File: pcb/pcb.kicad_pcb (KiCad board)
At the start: 2 copper layers, 30 parts, among them J1 Barrel_Jack_Switch, Q1 RQ5P010SN, SW1 SW_SPST, SW2 SW_SPST, SW3 SW_SPST, U1 L7805, U2 MCP1406/07, U3 MCP7940N-xSN, U4 Pico, Y1 Crystal

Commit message: finished routing
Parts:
- added C12: 6pF, Capacitor_SMD:C_1206_3216Metric_Pad1.33x1.80mm_HandSolder, F.Cu at (133.7, 151.8)
- added C13: 6pF, Capacitor_SMD:C_1206_3216Metric_Pad1.33x1.80mm_HandSolder, F.Cu at (133.7, 145.7)
- added H1: MountingHole_Pad, MountingHole:MountingHole_3.2mm_M3_DIN965_Pad, F.Cu at (144.8, 57.1)
- added J2: Conn_01x05_Pin, Connector_PinHeader_2.54mm:PinHeader_1x05_P2.54mm_Vertical, F.Cu at (121.9, 89.0)
- added J3: Conn_01x03_Pin, Connector_PinHeader_2.54mm:PinHeader_1x03_P2.54mm_Vertical, F.Cu at (114.3, 93.2)
- added J4: Conn_01x05_Pin, Connector_PinHeader_2.54mm:PinHeader_1x05_P2.54mm_Horizontal, F.Cu at (139.8, 164.2)
- added J5: Conn_01x03_Pin, Connector_PinHeader_2.54mm:PinHeader_1x03_P2.54mm_Horizontal, B.Cu at (142.3, 164.2)
- added R5: 10k, Resistor_SMD:R_1206_3216Metric_Pad1.30x1.75mm_HandSolder, F.Cu at (126.6, 143.4)
- added TP1: HV, TestPoint:TestPoint_THTPad_D1.5mm_Drill0.7mm, F.Cu at (146.7, 64.1)
- added TP2: 12V, TestPoint:TestPoint_THTPad_D1.5mm_Drill0.7mm, F.Cu at (122.6, 75.6)
- added TP3: 5V, TestPoint:TestPoint_THTPad_D1.5mm_Drill0.7mm, F.Cu at (116.8, 89.2)
- added TP4: GND, TestPoint:TestPoint_THTPad_D1.5mm_Drill0.7mm, F.Cu at (142.9, 84.5)
- added TP5: 3.3V, TestPoint:TestPoint_THTPad_D1.5mm_Drill0.7mm, F.Cu at (114.3, 89.2)
- added TP6: 5V, TestPoint:TestPoint_THTPad_D1.5mm_Drill0.7mm, F.Cu at (118.2, 112.4)
- added TP7: 3.3V, TestPoint:TestPoint_THTPad_D1.5mm_Drill0.7mm, F.Cu at (122.0, 117.5)
- added TP8: GND, TestPoint:TestPoint_THTPad_D1.5mm_Drill0.7mm, F.Cu at (116.9, 149.3)
- added U5: Pico, MCU_RaspberryPi_and_Boards:RPi_Pico_SMD, B.Cu at (136.0, 130.5)
- added V1: IV-18, vfd:IV-18, B.Cu at (130.8, 57.1)
- added mouse-bite-2.54mm-slot: VAL**, Panelization:mouse-bite-2.54mm-slot, F.Cu at (145.4, 102.9)
- added mouse-bite-2.54mm-slot: VAL**, Panelization:mouse-bite-2.54mm-slot, F.Cu at (116.2, 102.9)
- C10, C11: value 6pF -> 0.1uF
- D3: moved to B.Cu
- R2: value 10k -> 22
- U3: value MCP7940N-xSN -> MAX6921AWI; footprint Package_SO:SOIC-8_3.9x4.9mm_P1.27mm -> Package_SO:SOIC-28W_7.5x17.9mm_P1.27mm
- U4: value Pico -> MCP7940N-xSN; footprint MCU_RaspberryPi_and_Boards:RPi_Pico_SMD -> Package_SO:SOIC-8_3.9x4.9mm_P1.27mm
- Y1: value Crystal -> Crystal_GND3; footprint vfd:Crystal_DS26_D2.0mm_L6.0mm_Horizontal_SMT -> vfd:Crystal_DS26_D2.0mm_L6.0mm_Horizontal_Grounded_SMT
- moved U4 132.6 mm to (125.6, 148.6), turned to 180 degrees
- moved BT1 118.7 mm to (139.8, 127.0), turned to -90 degrees
- moved SW1 108.7 mm to (114.4, 144.2), turned to 90 degrees
- moved L1 107.4 mm to (133.3, 68.7), turned to -90 degrees
- moved C11 105.8 mm to (131.8, 154.2)
- moved C10 105.7 mm to (146.7, 37.8), turned to -90 degrees
- moved C9 101.9 mm to (146.7, 44.1), turned to -90 degrees
- moved Q1 100.8 mm to (138.7, 79.7)
- moved Y1 99.9 mm to (133.1, 149.7), turned to 90 degrees
- moved R3 96.2 mm to (126.6, 140.8), turned to 180 degrees
- moved C5 94.9 mm to (144.8, 80.3), turned to -90 degrees
- moved SW2 94.3 mm to (114.4, 134.0), turned to 90 degrees
- moved R4 91.1 mm to (126.6, 138.3), turned to 180 degrees
- moved C2 90.4 mm to (126.7, 71.1), turned to 180 degrees
- moved C4 85.8 mm to (142.9, 70.5), turned to 90 degrees
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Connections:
- net Net-(Q1-G) renamed /GATE
- BT1 pad 2: GND -> GNDA
- C10 pad 1: Net-(U3-X1) -> /30-50V
- C11 pad 1: Net-(U3-X2) -> +3.3VA
- C11 pad 2: GND -> GNDA
- C9 pad 1: +3.3V -> GND
- C9 pad 2: GND -> +3.3V
- D3 pad 2: +5V -> +5VA
- R2 pad 1: +3.3V -> +5V
- R2 pad 2: /SCL -> Net-(R2-Pad2)
- R3 pad 1: +3.3V -> +3.3VA
- R3 pad 2: /SDA -> /SCL
- R4 pad 1: +3.3V -> +3.3VA
- R4 pad 2: /MFP -> /SDA
- SW1 pad 2: GND -> GNDA
- SW2 pad 2: GND -> GNDA
- SW3 pad 2: GND -> GNDA
- U3 pad 1: Net-(U3-X1) -> /30-50V
- U3 pad 2: Net-(U3-X2) -> unconnected-(U3-DOUT-Pad2)
- U3 pad 3: Net-(BT1-+) -> unconnected-(U3-OUT19-Pad3)
- U3 pad 4: GND -> unconnected-(U3-OUT18-Pad4)
- U3 pad 5: /SDA -> unconnected-(U3-OUT17-Pad5)
- U3 pad 6: /SCL -> Net-(U3-OUT16)
- U3 pad 7: /MFP -> Net-(U3-OUT15)
- U3 pad 8: +3.3V -> Net-(U3-OUT14)
- U4 pad 1: unconnected-(U4-GPIO0-Pad1) -> Net-(U4-X1)
- U4 pad 2: unconnected-(U4-GPIO1-Pad2) -> Net-(U4-X2)
- U4 pad 3: GND -> Net-(BT1-+)
- U4 pad 4: unconnected-(U4-GPIO2-Pad4) -> GNDA
- U4 pad 5: unconnected-(U4-GPIO3-Pad5) -> /SDA
- U4 pad 6: unconnected-(U4-GPIO4-Pad6) -> /SCL
- U4 pad 7: unconnected-(U4-GPIO5-Pad7) -> /MFP
- U4 pad 8: GND -> +3.3VA
- Y1 pad 1: Net-(U3-X2) -> Net-(U4-X1)
- Y1 pad 2: Net-(U3-X1) -> Net-(U4-X2)
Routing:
- net +3.3VA: track 0.00 -> 87.8 mm
- net /DATA: track 0.00 -> 85.0 mm, vias 0 -> 1
- net +3.3V: track 0.00 -> 83.8 mm
- net +5VA: track 0.00 -> 74.6 mm
- net /BLANK: track 0.00 -> 64.9 mm, vias 0 -> 1
- net /LATCH: track 0.00 -> 62.3 mm, vias 0 -> 1
- net +5V: track 0.00 -> 60.5 mm
- net /CLOCK: track 0.00 -> 60.4 mm, vias 0 -> 1
- net Net-(BT1-+): track 0.00 -> 52.1 mm
- net +12V: track 0.00 -> 45.5 mm
- net /30-50V: track 0.00 -> 44.9 mm
- net /MCU_CLOCK: track 0.00 -> 43.9 mm
- net /MCU_DATA: track 0.00 -> 41.4 mm
- net /MCU_LATCH: track 0.00 -> 35.8 mm
- net Net-(U3-OUT16): track 0.00 -> 33.6 mm, vias 0 -> 1
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- added copper zone on F.Cu, net +12V
- added copper zone on F.Cu, net /30-50V
- added copper zone on F.Cu, net /GATE
- added copper zone on B.Cu, net GND
- added copper zone on F.Cu, net GND
- added copper zone on F.Cu, net GNDA
- added copper zone on F.Cu, net Net-(D1-A)
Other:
- board outline added: 38.1 x 134 mm

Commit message: finished pcb
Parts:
- added Q2: IRLML6244, Package_TO_SOT_SMD:SOT-23_Handsoldering, F.Cu at (129.8, 54.1)
- added R6: 10k, Resistor_SMD:R_1206_3216Metric_Pad1.30x1.75mm_HandSolder, F.Cu at (126.5, 143.5)
- J2: value Conn_01x05_Pin -> Conn_01x06_Pin; footprint Connector_PinHeader_2.54mm:PinHeader_1x05_P2.54mm_Vertical -> Connector_PinHeader_2.54mm:PinHeader_1x06_P2.54mm_Vertical
- J4: value Conn_01x05_Pin -> Conn_01x06_Pin; footprint Connector_PinHeader_2.54mm:PinHeader_1x05_P2.54mm_Horizontal -> Connector_PinHeader_2.54mm:PinHeader_1x06_P2.54mm_Horizontal
- R3: value 10k -> 470
- moved R3 81.1 mm to (133.3, 60.0), turned to 90 degrees
- moved R5 4.96 mm to (126.5, 138.4)
- moved R4 2.67 mm to (126.5, 141.0)
- moved J1 2.62 mm to (138.4, 91.2)
- moved TP4 2.29 mm to (141.0, 83.2)
- moved SW1 2.12 mm to (112.4, 144.8)
- moved SW2 2.04 mm to (112.4, 134.0)
- moved SW3 2.04 mm to (112.4, 123.2)
- moved TP7 1.91 mm to (122.0, 119.4)
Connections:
- net Net-(U3-OUT0) renamed /D2
- net Net-(U3-OUT1) renamed /D4
- net Net-(U3-OUT10) renamed /G
- net Net-(U3-OUT11) renamed /B
- net Net-(U3-OUT12) renamed /F
- net Net-(U3-OUT13) renamed /E
- net Net-(U3-OUT14) renamed /C
- net Net-(U3-OUT15) renamed /D
- net Net-(U3-OUT16) renamed /DP
- net Net-(U3-OUT2) renamed /D6
- net Net-(U3-OUT3) renamed /D7
- net Net-(U3-OUT4) renamed /D8
- net Net-(U3-OUT5) renamed /D5
- net Net-(U3-OUT6) renamed /D3
- net Net-(U3-OUT7) renamed /D1
- net Net-(U3-OUT8) renamed /D9
- net Net-(U3-OUT9) renamed /A
- R3 pad 1: +3.3VA -> /FIL
- R3 pad 2: /SCL -> Net-(Q2-G)
- R4 pad 2: /SDA -> /SCL
- R5 pad 2: /MFP -> /SDA
- U5 pad 24: unconnected-(U5-GPIO18-Pad24) -> /MCU_FIL
- V1 pad 13: GND -> Net-(Q2-D)
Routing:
- net /FIL: track 0.00 -> 38.1 mm, vias 0 -> 1
- net /MCU_FIL: track 0.00 -> 21.8 mm
- net Net-(Q2-G): track 0.00 -> 10.3 mm
- net /30-50V: track 44.9 -> 51.8 mm
- net GND: track 15.3 -> 11.6 mm, vias 3 -> 5
- net Net-(Q2-D): track 0.00 -> 3.54 mm
- net +12V: track 45.5 -> 48.5 mm
- net GNDA: track 17.4 -> 19.9 mm
- net /SWITCH3: track 13.3 -> 15.4 mm
- net /SWITCH2: track 15.7 -> 17.7 mm
- net +3.3VA: track 87.8 -> 85.8 mm
- net /SWITCH1: track 21.2 -> 22.7 mm
- net +5V: track 60.5 -> 61.6 mm
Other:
- board size 38.1 x 134 mm -> 43.2 x 134 mm

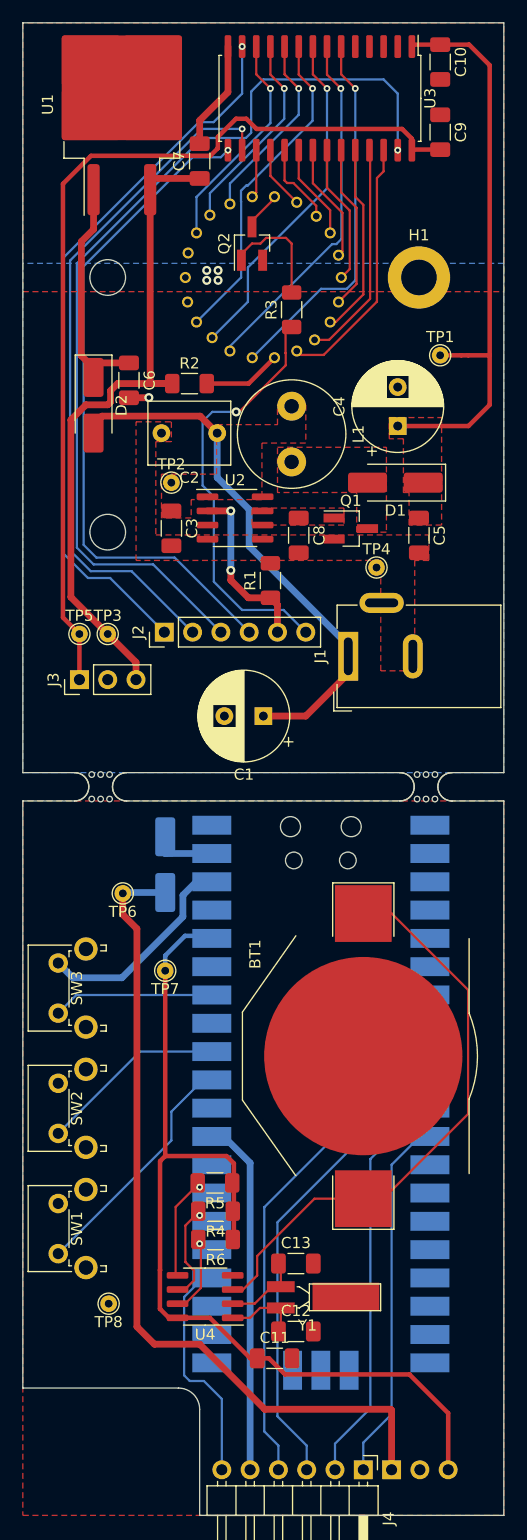
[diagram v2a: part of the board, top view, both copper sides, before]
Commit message: fixed some traces
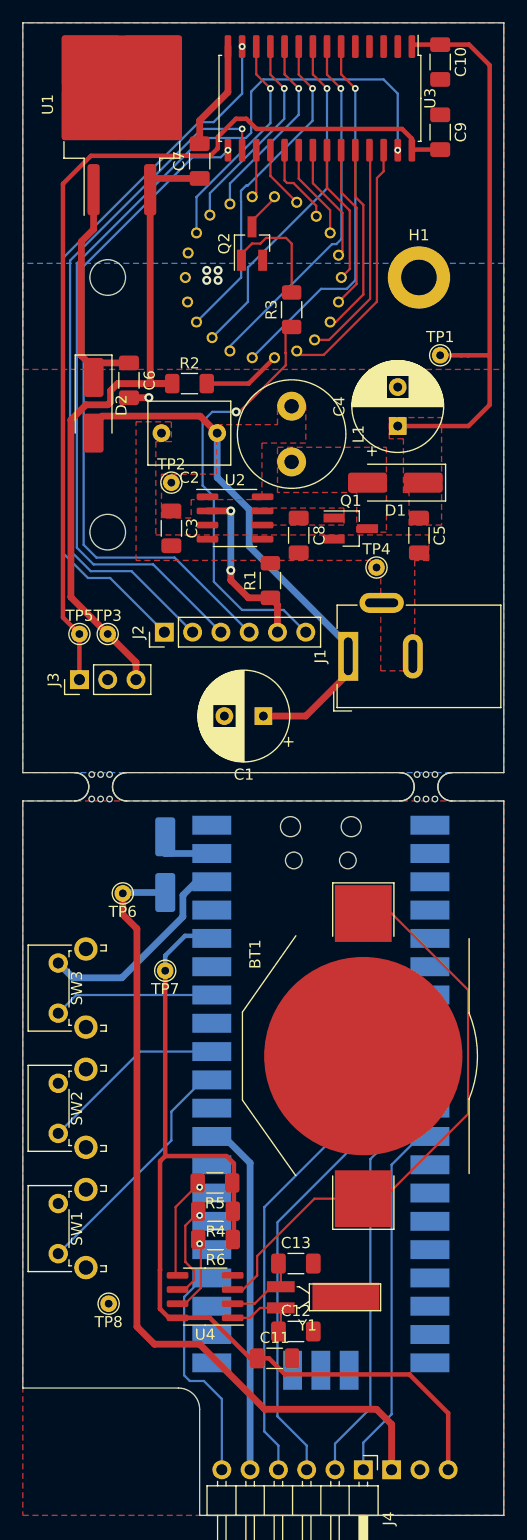
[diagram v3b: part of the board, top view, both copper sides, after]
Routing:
- net +5VA: track 74.6 -> 73.8 mm
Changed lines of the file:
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@@
   (segment (start 132.378 147.7462) (end 131.7815 147.7462) (width 0.2032) (layer "F.Cu") (net 21))
   (segment (start 132.1685 145.669) (end 132.378 145.8785) (width 0.2032) (layer "F.Cu") (net 21))
-  (segment (start 142.3225 158.8325) (end 142.3225 164.18) (width 0.6096) (layer "F.Cu") (net 22))
-  (segment (start 130.937 158.75) (end 142.24 158.75) (width 0.6096) (layer "F.Cu") (net 22))
+  (segment (start 140.97 158.75) (end 142.3225 160.1025) (width 0.6096) (layer "F.Cu") (net 22))
+  (segment (start 118.1925 114.3452) (end 119.4625 115.6152) (width 0.6096) (layer "F.Cu") (net 22))
+  (segment (start 125.095 152.908) (end 130.937 158.75) (width 0.6096) (layer "F.Cu") (net 22))
   (segment (start 119.4625 115.6152) (end 119.4625 151.3395) (width 0.6096) (layer "F.Cu") (net 22))
+  (segment (start 142.3225 160.1025) (end 142.3225 164.18) (width 0.6096) (layer "F.Cu") (net 22))
+  (segment (start 118.1925 112.4402) (end 118.1925 114.3452) (width 0.6096) (layer "F.Cu") (net 22))
   (segment (start 119.4625 151.3395) (end 121.031 152.908) (width 0.6096) (layer "F.Cu") (net 22))
-  (segment (start 125.095 152.908) (end 130.937 158.75) (width 0.6096) (layer "F.Cu") (net 22))
+  (segment (start 130.937 158.75) (end 140.97 158.75) (width 0.6096) (layer "F.Cu") (net 22))
   (segment (start 121.031 152.908) (end 125.095 152.908) (width 0.6096) (layer "F.Cu") (net 22))
-  (segment (start 142.24 158.75) (end 142.3225 158.8325) (width 0.6096) (layer "F.Cu") (net 22))
-  (segment (start 118.1925 112.4402) (end 118.1925 114.3452) (width 0.6096) (layer "F.Cu") (net 22))
-  (segment (start 118.1925 114.3452) (end 119.4625 115.6152) (width 0.6096) (layer "F.Cu") (net 22))
   (segment (start 118.2725 112.3602) (end 118.1925 112.4402) (width 0.6096) (layer "B.Cu") (net 22))
   (segment (start 122.0025 112.3602) (end 118.2725 112.3602) (width 0.6096) (layer "B.Cu") (net 22))
@@
     (polygon
       (pts
-        (xy 109.22 58.42)
-        (xy 152.4 58.42)
+        (xy 109.22 65.405)
+        (xy 152.4 65.405)
         (xy 152.4 34.29)
         (xy 109.22 34.29)

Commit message: finished pcb
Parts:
- BT1: value Battery_Cell -> CR2032
- R1: value 10k -> 100k
- Y1: value Crystal_GND3 -> 32.768KHZ
- moved TP4 7.73 mm to (148.6, 81.9)
- moved BT1 1.82 mm to (141.6, 127.0)
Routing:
- net GND: track 11.6 -> 15.4 mm
- net Net-(BT1-+): track 52.1 -> 55.0 mm

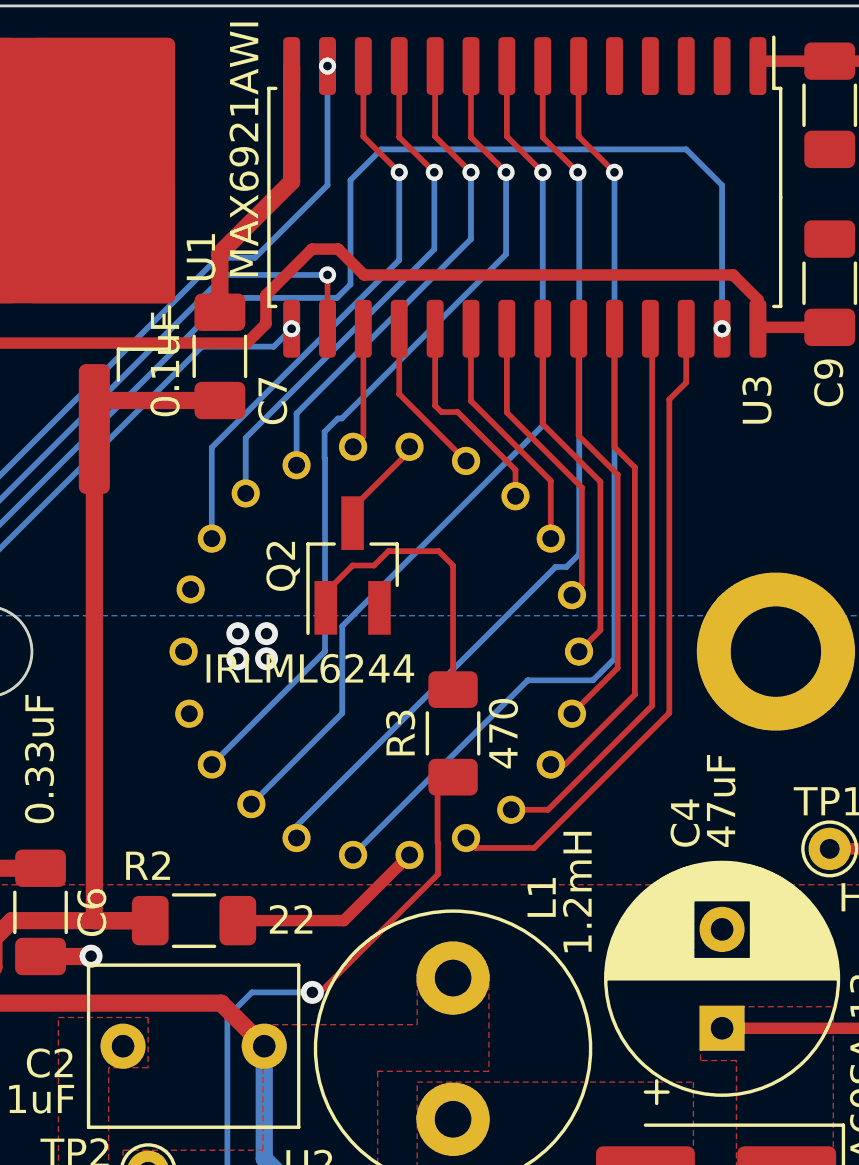
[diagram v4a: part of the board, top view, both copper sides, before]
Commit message: rotated display
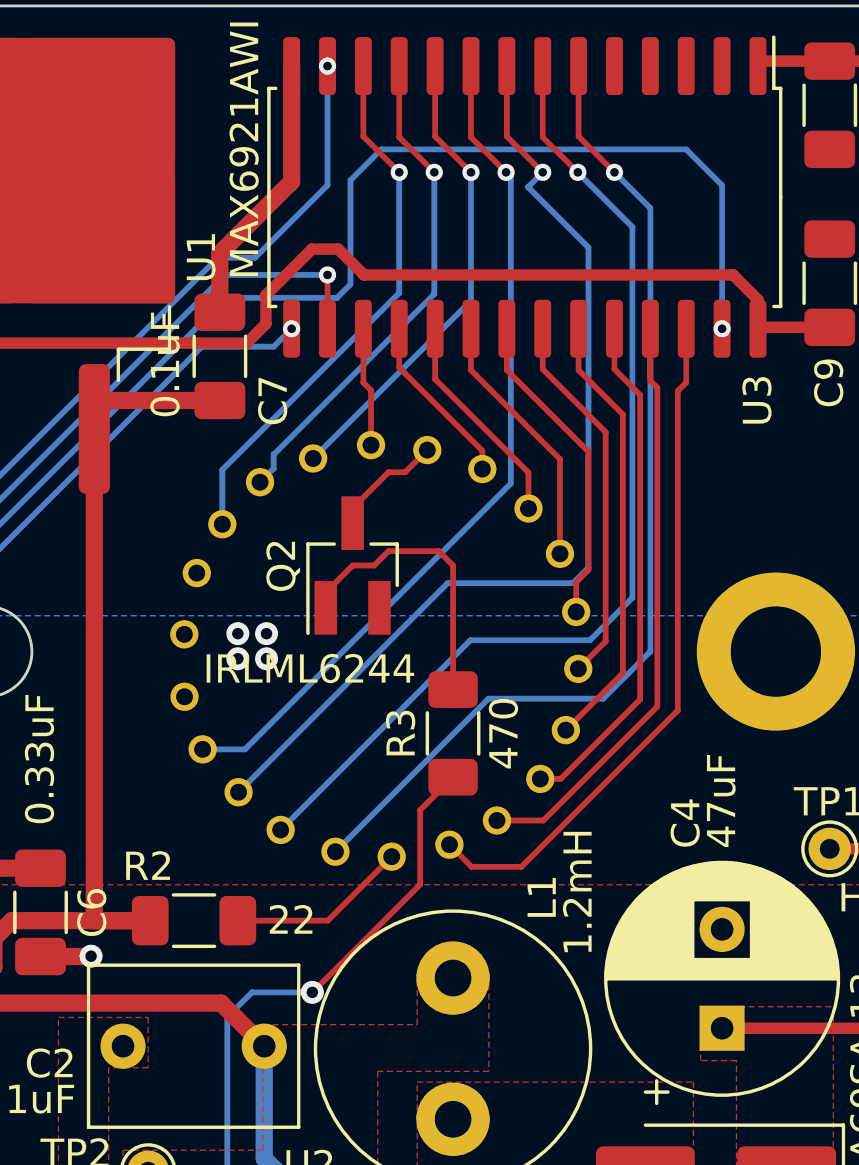
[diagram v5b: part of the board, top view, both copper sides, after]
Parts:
- turned V1 to 85 degrees
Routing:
- net /C: track 30.9 -> 35.1 mm
- net /D: track 32.2 -> 36.0 mm
- net /DP: track 33.6 -> 35.9 mm
- net /D2: track 23.2 -> 24.4 mm
- net Net-(Q2-D): track 3.54 -> 4.56 mm
- net /D6: track 17.3 -> 18.2 mm
- net /D4: track 19.9 -> 20.8 mm
- net /D7: track 14.9 -> 15.7 mm
- net /D8: track 12.6 -> 13.4 mm
- net /D5: track 10.7 -> 11.4 mm
- net /D3: track 8.60 -> 9.27 mm
- net /G: track 20.0 -> 19.3 mm
- net Net-(R2-Pad2): track 7.04 -> 6.39 mm
- net /B: track 18.4 -> 17.8 mm
- net /D9: track 5.66 -> 6.19 mm
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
